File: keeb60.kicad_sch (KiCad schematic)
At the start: 0 parts

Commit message: Add power lines
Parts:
- added U1: nice_nano, symbol nice_nano:nice_nano
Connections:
- new net +5V: U1.21 (VCC)
- new net GND: U1.23 (GND)

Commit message: Add matrix
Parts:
- removed U1: nice_nano, symbol nice_nano:nice_nano
- added D0, D1, D10, D11, D12, D13, D14, D15, D16, D17, D18, D19, D2, D20, D21, D22, D23, D24, D25, D26, D27, D28, D29, D3, D30, D31, D32, D33, D34, D35, D36, D37, D38, D39, D4, D41, D42, D44, D45, D46, D47, D48, D49, D5, D50, D51, D52, D53, D55, D56, D57, D58, D6, D62, D66, D67, D68, D69, D7, D8, D9: D, symbol Device:D
- added K000: Esc, symbol Switch:SW_Push
- added K001: 1, symbol Switch:SW_Push
- added K002: 2, symbol Switch:SW_Push
- added K003: 3, symbol Switch:SW_Push
- added K004: 4, symbol Switch:SW_Push
- added K005: 5, symbol Switch:SW_Push
- added K006: 6, symbol Switch:SW_Push
- added K007: 7, symbol Switch:SW_Push
- added K008: 8, symbol Switch:SW_Push
- added K009: 9, symbol Switch:SW_Push
- added K010: 0, symbol Switch:SW_Push
- added K011: _, symbol Switch:SW_Push
- added K012: =, symbol Switch:SW_Push
- added K013: Backspace, symbol Switch:SW_Push
- added K100: Tab, symbol Switch:SW_Push
- added K101: Q, symbol Switch:SW_Push
- added K102: W, symbol Switch:SW_Push
- added K103: E, symbol Switch:SW_Push
- added K104: R, symbol Switch:SW_Push
- added K105: T, symbol Switch:SW_Push
- added K106: Y, symbol Switch:SW_Push
- added K107: U, symbol Switch:SW_Push
- added K108: I, symbol Switch:SW_Push
- added K109: O, symbol Switch:SW_Push
- added K110: P, symbol Switch:SW_Push
- added K111: [, symbol Switch:SW_Push
- added K112: ], symbol Switch:SW_Push
- added K113: |, symbol Switch:SW_Push
- added K200: Caps Lock, symbol Switch:SW_Push
- added K201: A, symbol Switch:SW_Push
- added K202: S, symbol Switch:SW_Push
- added K203: D, symbol Switch:SW_Push
- added K204: F, symbol Switch:SW_Push
- added K205: G, symbol Switch:SW_Push
- added K206: H, symbol Switch:SW_Push
- added K207: J, symbol Switch:SW_Push
- added K208: K, symbol Switch:SW_Push
- added K209: L, symbol Switch:SW_Push
- added K210: ;, symbol Switch:SW_Push
- added K211, K309: ,, symbol Switch:SW_Push
- added K213: Enter, symbol Switch:SW_Push
- added K300, K313: Shift, symbol Switch:SW_Push
- added K302: Z, symbol Switch:SW_Push
- added K303: X, symbol Switch:SW_Push
- added K304: C, symbol Switch:SW_Push
- added K305: V, symbol Switch:SW_Push
- added K306: B, symbol Switch:SW_Push
- added K307: N, symbol Switch:SW_Push
- added K308: M, symbol Switch:SW_Push
- added K310: ., symbol Switch:SW_Push
- added K311: /, symbol Switch:SW_Push
- added K400, K413: Ctrl, symbol Switch:SW_Push
- added K401, K411: Option, symbol Switch:SW_Push
- added K402, K410: Command, symbol Switch:SW_Push
- added K406: Space, symbol Switch:SW_Push
- added K412: Function, symbol Switch:SW_Push
- added U1: ProMicro, Zodiark:ProMicro_rev2, symbol TheOneProMicro:ProMicro_2-Lily58-cache
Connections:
- new net: D41.2 (A), K213.1
- new net: D15.2 (A), K101.1
- new net: D44.2 (A), K302.1
- new net: D55.2 (A), K313.1
- new net: D45.2 (A), K303.1
- new net: D46.2 (A), K304.1
- new net: D42.2 (A), K300.1
- new net: D30.2 (A), K202.1
- new net: D34.2 (A), K206.1
- new net: D16.2 (A), K102.1
- new net: D4.2 (A), K004.1
- new net: D51.2 (A), K309.1
- new net: D3.2 (A), K003.1
- new net: D67.2 (A), K411.1
- new net: D36.2 (A), K208.1
- new net: D58.2 (A), K402.1
- new net: D62.2 (A), K406.1
- new net: D49.2 (A), K307.1
- new net: D12.2 (A), K012.1
- new net: D28.2 (A), K200.1
- new net: D9.2 (A), K009.1
- new net: D31.2 (A), K203.1
- new net: D57.2 (A), K401.1
- new net: D32.2 (A), K204.1
- new net: D0.2 (A), K000.1
- new net: D66.2 (A), K410.1
- new net: D11.2 (A), K011.1
- new net: D10.2 (A), K010.1
- new net: D8.2 (A), K008.1
- new net: D6.2 (A), K006.1
- new net: D18.2 (A), K104.1
- new net: D47.2 (A), K305.1
- new net: D24.2 (A), K110.1
- new net: D7.2 (A), K007.1
- new net: D52.2 (A), K310.1
- new net: D22.2 (A), K108.1
- new net: D19.2 (A), K105.1
- new net: D68.2 (A), K412.1
- new net: D29.2 (A), K201.1
- new net: D53.2 (A), K311.1
- new net: D26.2 (A), K112.1
- new net: D27.2 (A), K113.1
- new net: D14.2 (A), K100.1
- new net: D17.2 (A), K103.1
- new net: D39.2 (A), K211.1
- new net: D37.2 (A), K209.1
- new net: D2.2 (A), K002.1
- new net: D21.2 (A), K107.1
- new net: D5.2 (A), K005.1
- new net: D56.2 (A), K400.1
- new net: D48.2 (A), K306.1
- new net: D25.2 (A), K111.1
- new net: D20.2 (A), K106.1
- new net: D33.2 (A), K205.1
- new net: D35.2 (A), K207.1
- new net: D23.2 (A), K109.1
- new net: D38.2 (A), K210.1
- new net: D13.2 (A), K013.1
- new net: D50.2 (A), K308.1
- new net: D1.2 (A), K001.1
- new net: D69.2 (A), K413.1
- new net Col0: K000.2, K100.2, K200.2, K300.2, K400.2, U1.1 (GP0(TX))
- new net Col1: K001.2, K101.2, K201.2, K401.2, U1.2 (GP1(RX))
- new net Col10: K010.2, K110.2, K210.2, K310.2, K410.2, U1.17 (GP26(A0))
- new net Col11: K011.2, K111.2, K211.2, K311.2, K411.2, U1.18 (GP27(A1))
- new net Col12: K012.2, K112.2, K412.2, U1.19 (GP28(A2))
- new net Col13: K013.2, K113.2, K213.2, K313.2, K413.2, U1.20 (GP29(A3))
- new net Col2: K002.2, K102.2, K202.2, K302.2, K402.2, U1.5 (SDA(GP2))
- new net Col3: K003.2, K103.2, K203.2, K303.2, U1.6 (SCL(GP3))
- new net Col4: K004.2, K104.2, K204.2, K304.2, U1.7 (GP4)
- new net Col5: K005.2, K105.2, K205.2, K305.2, U1.8 (GP5)
- new net Col6: K006.2, K106.2, K206.2, K306.2, K406.2, U1.9 (GP6)
- new net Col7: K007.2, K107.2, K207.2, K307.2, U1.14 (GP23)
- new net Col8: K008.2, K108.2, K208.2, K308.2, U1.15 (GP20)
- new net Col9: K009.2, K109.2, K209.2, K309.2, U1.16 (GP22)
- new net Row0: D0.1 (K), D1.1 (K), D10.1 (K), D11.1 (K), D12.1 (K), D13.1 (K), D2.1 (K), D3.1 (K), D4.1 (K), D5.1 (K), D6.1 (K), D7.1 (K), D8.1 (K), D9.1 (K), U1.10 (GP7)
- new net Row1: D14.1 (K), D15.1 (K), D16.1 (K), D17.1 (K), D18.1 (K), D19.1 (K), D20.1 (K), D21.1 (K), D22.1 (K), D23.1 (K), D24.1 (K), D25.1 (K), D26.1 (K), D27.1 (K), U1.11 (GP8)
- new net Row2: D28.1 (K), D29.1 (K), D30.1 (K), D31.1 (K), D32.1 (K), D33.1 (K), D34.1 (K), D35.1 (K), D36.1 (K), D37.1 (K), D38.1 (K), D39.1 (K), D41.1 (K), U1.12 (GP9)
- new net Row3: D42.1 (K), D44.1 (K), D45.1 (K), D46.1 (K), D47.1 (K), D48.1 (K), D49.1 (K), D50.1 (K), D51.1 (K), D52.1 (K), D53.1 (K), D55.1 (K), U1.13 (GP21)
- new net Row4: D56.1 (K), D57.1 (K), D58.1 (K), D62.1 (K), D66.1 (K), D67.1 (K), D68.1 (K), D69.1 (K)

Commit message: Start assigning footprints
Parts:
- K000, K001: footprint (none) -> MX_Hotswap:MX-Hotswap-1U
- U1: footprint Zodiark:ProMicro_rev2 -> TheOneProMicro-main:TheOneProMicro
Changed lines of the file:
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@@
 			)
 		)
-		(property "Footprint" ""
+		(property "Footprint" "MX_Hotswap:MX-Hotswap-1U"
 			(at 57.15 78.74 0)
 			(effects
@@
 			)
 		)
-		(property "Footprint" "Zodiark:ProMicro_rev2"
+		(property "Footprint" "TheOneProMicro-main:TheOneProMicro"
 			(at 38.1 41.91 0)
 			(effects
@@
 			)
 		)
-		(property "Footprint" ""
+		(property "Footprint" "MX_Hotswap:MX-Hotswap-1U"
 			(at 72.39 78.74 0)
 			(effects

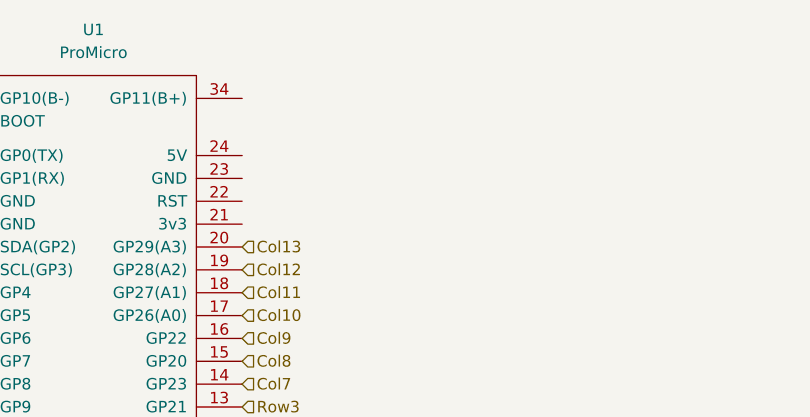
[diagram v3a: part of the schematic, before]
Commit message: Add footprints
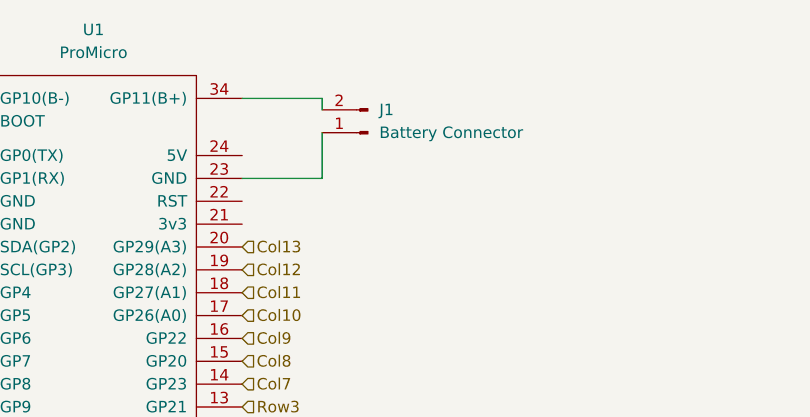
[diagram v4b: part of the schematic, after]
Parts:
- added J1: Battery Connector, Connector_JST:JST_XH_B2B-XH-A_1x02_P2.50mm_Vertical, symbol Connector:Conn_01x02_Pin
- D0, D1, D10, D11, D12, D13, D14, D15, D16, D17, D18, D19, D2, D20, D21, D22, D23, D24, D25, D26, D27, D28, D29, D3, D30, D31, D32, D33, D34, D35, D36, D37, D38, D39, D4, D41, D42, D44, D45, D46, D47, D48, D49, D5, D50, D51, D52, D53, D55, D56, D57, D58, D6, D62, D66, D67, D68, D69, D7, D8, D9: footprint (none) -> Diode_THT:D_DO-35_SOD27_P7.62mm_Horizontal
- K002, K003, K004, K005, K006, K007, K008, K009, K010, K011, K012, K101, K102, K103, K104, K105, K106, K107, K108, K109, K110, K111, K112, K201, K202, K203, K204, K205, K206, K207, K208, K209, K210, K211, K302, K303, K304, K305, K306, K307, K308, K309, K310, K311: footprint (none) -> MX_Hotswap:MX-Hotswap-1U
- K013: footprint (none) -> MX_Hotswap:MX-Hotswap-2U
- K100, K113: footprint (none) -> MX_Hotswap:MX-Hotswap-1.5U
- K200: footprint (none) -> MX_Hotswap:MX-Hotswap-1.75U
- K213, K300: footprint (none) -> MX_Hotswap:MX-Hotswap-2.25U
- K313: footprint (none) -> MX_Hotswap:MX-Hotswap-2.75U
- K400, K401, K402, K410, K411, K412, K413: footprint (none) -> MX_Hotswap:MX-Hotswap-1.25U
- K406: footprint (none) -> MX_Hotswap:MX-Hotswap-6.25U-ReversedStabilizers
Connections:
- net at U1.23 (GND): now also J1.1 (Pin_1)
- net at U1.34 (GP11(B+)): now also J1.2 (Pin_2)

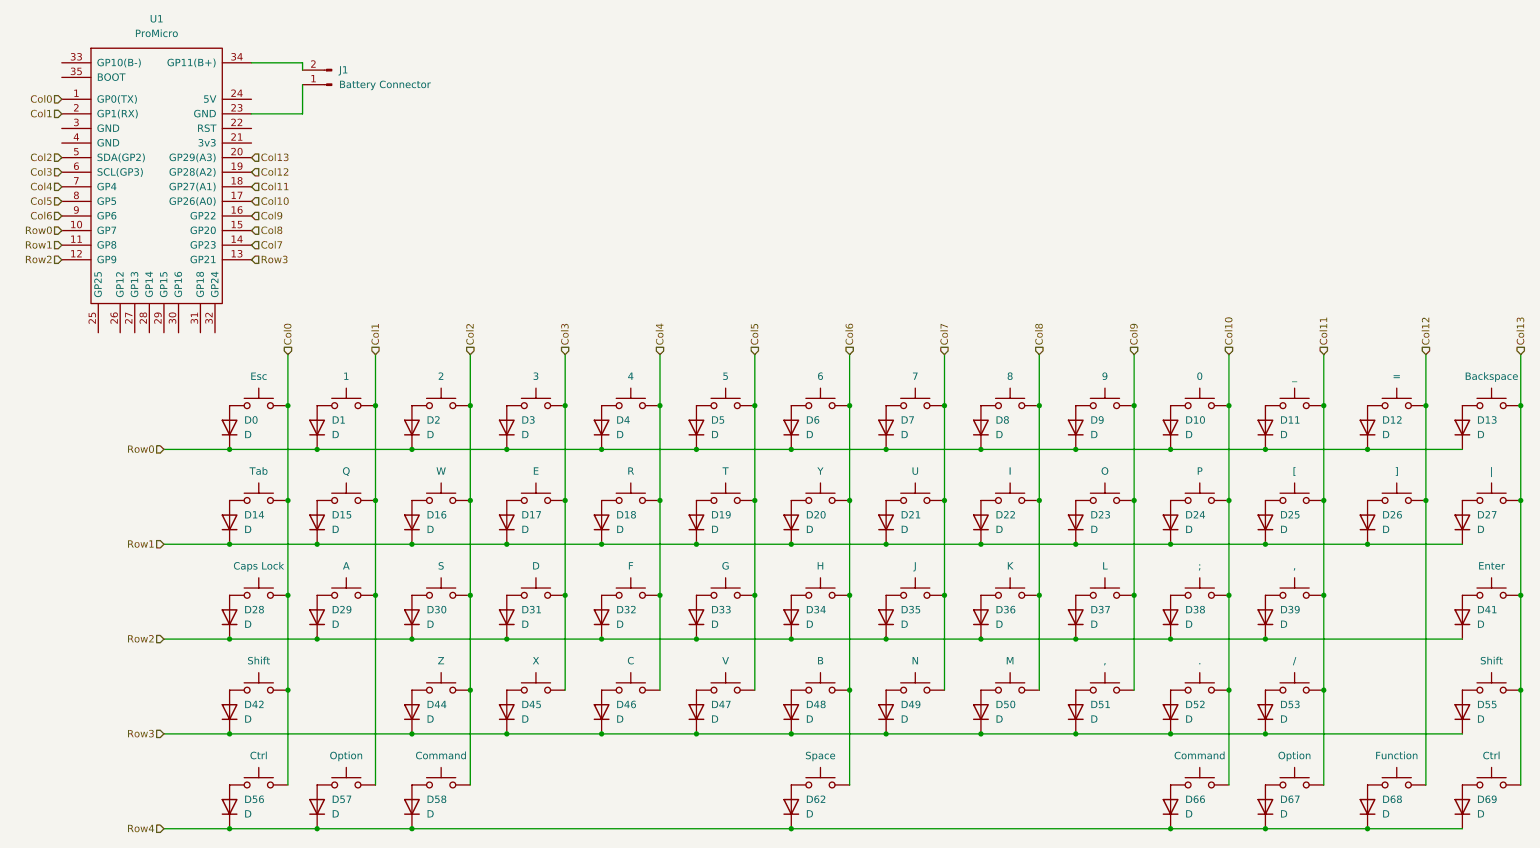
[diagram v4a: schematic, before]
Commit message: Switch to SMA diodes, start laying out board
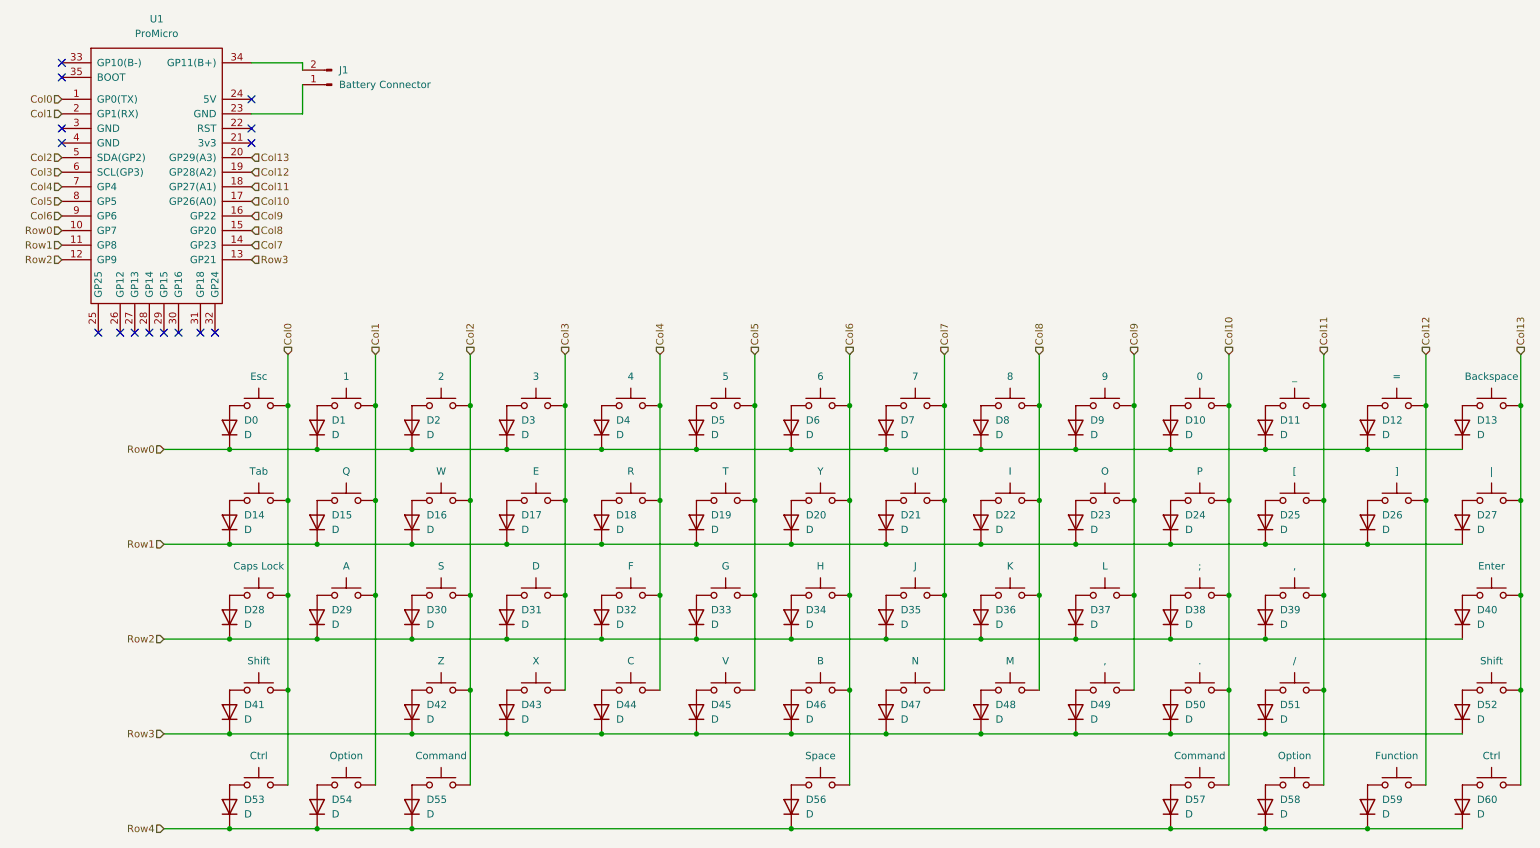
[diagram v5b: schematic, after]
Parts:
- D0, D1, D10, D11, D12, D13, D14, D15, D16, D17, D18, D19, D2, D20, D21, D22, D23, D24, D25, D26, D27, D28, D29, D3, D30, D31, D32, D33, D34, D35, D36, D37, D38, D39, D4, D5, D6, D7, D8, D9: footprint Diode_THT:D_DO-35_SOD27_P7.62mm_Horizontal -> Diode_SMD:D_SOD-123
- D40: renamed from D41; footprint Diode_THT:D_DO-35_SOD27_P7.62mm_Horizontal -> Diode_SMD:D_SOD-123
- D41: renamed from D42; footprint Diode_THT:D_DO-35_SOD27_P7.62mm_Horizontal -> Diode_SMD:D_SOD-123
- D42: renamed from D44; footprint Diode_THT:D_DO-35_SOD27_P7.62mm_Horizontal -> Diode_SMD:D_SOD-123
- D43: renamed from D45; footprint Diode_THT:D_DO-35_SOD27_P7.62mm_Horizontal -> Diode_SMD:D_SOD-123
- D44: renamed from D46; footprint Diode_THT:D_DO-35_SOD27_P7.62mm_Horizontal -> Diode_SMD:D_SOD-123
- D45: renamed from D47; footprint Diode_THT:D_DO-35_SOD27_P7.62mm_Horizontal -> Diode_SMD:D_SOD-123
- D46: renamed from D48; footprint Diode_THT:D_DO-35_SOD27_P7.62mm_Horizontal -> Diode_SMD:D_SOD-123
- D47: renamed from D49; footprint Diode_THT:D_DO-35_SOD27_P7.62mm_Horizontal -> Diode_SMD:D_SOD-123
- D48: renamed from D50; footprint Diode_THT:D_DO-35_SOD27_P7.62mm_Horizontal -> Diode_SMD:D_SOD-123
- D49: renamed from D51; footprint Diode_THT:D_DO-35_SOD27_P7.62mm_Horizontal -> Diode_SMD:D_SOD-123
- D50: renamed from D52; footprint Diode_THT:D_DO-35_SOD27_P7.62mm_Horizontal -> Diode_SMD:D_SOD-123
- D51: renamed from D53; footprint Diode_THT:D_DO-35_SOD27_P7.62mm_Horizontal -> Diode_SMD:D_SOD-123
- D52: renamed from D55; footprint Diode_THT:D_DO-35_SOD27_P7.62mm_Horizontal -> Diode_SMD:D_SOD-123
- D53: renamed from D56; footprint Diode_THT:D_DO-35_SOD27_P7.62mm_Horizontal -> Diode_SMD:D_SOD-123
- D54: renamed from D57; footprint Diode_THT:D_DO-35_SOD27_P7.62mm_Horizontal -> Diode_SMD:D_SOD-123
- D55: renamed from D58; footprint Diode_THT:D_DO-35_SOD27_P7.62mm_Horizontal -> Diode_SMD:D_SOD-123
- D56: renamed from D62; footprint Diode_THT:D_DO-35_SOD27_P7.62mm_Horizontal -> Diode_SMD:D_SOD-123
- D57: renamed from D66; footprint Diode_THT:D_DO-35_SOD27_P7.62mm_Horizontal -> Diode_SMD:D_SOD-123
- D58: renamed from D67; footprint Diode_THT:D_DO-35_SOD27_P7.62mm_Horizontal -> Diode_SMD:D_SOD-123
- D59: renamed from D68; footprint Diode_THT:D_DO-35_SOD27_P7.62mm_Horizontal -> Diode_SMD:D_SOD-123
- D60: renamed from D69; footprint Diode_THT:D_DO-35_SOD27_P7.62mm_Horizontal -> Diode_SMD:D_SOD-123
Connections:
- no-connect marks 0 -> 15

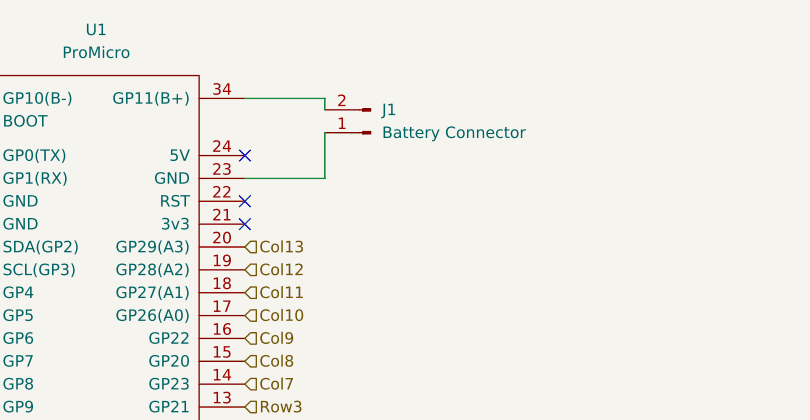
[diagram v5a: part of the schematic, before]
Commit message: Remove JST from board
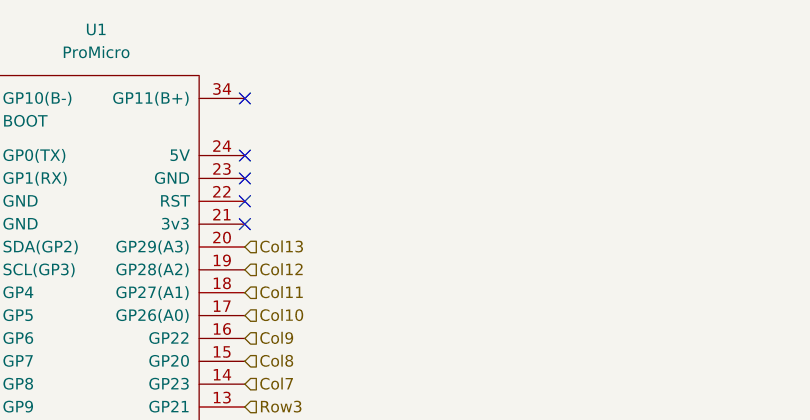
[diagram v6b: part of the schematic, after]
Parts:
- removed J1: Battery Connector, Connector_JST:JST_XH_B2B-XH-A_1x02_P2.50mm_Vertical, symbol Connector:Conn_01x02_Pin
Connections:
- no-connect marks 15 -> 17
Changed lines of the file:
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@@
 	)
 	(no_connect
+		(at 55.88 33.02)
+	)
+	(no_connect
 		(at 40.64 71.12)
 	)
@@
 	)
 	(no_connect
+		(at 55.88 24.13)
+	)
+	(no_connect
 		(at 49.53 71.12)
 	)
@@
 	(wire
 		(pts
-			(xy 55.88 33.02) (xy 64.77 33.02)
-		)
-		(stroke
-			(width 0)
-			(type default)
-		)
-	)
-	(wire
-		(pts
 			(xy 242.57 133.35) (xy 242.57 149.86)
 		)
@@
 	(wire
 		(pts
-			(xy 55.88 24.13) (xy 64.77 24.13)
-		)
-		(stroke
-			(width 0)
-			(type default)
-		)
-	)
-	(wire
-		(pts
 			(xy 232.41 157.48) (xy 250.19 157.48)
 		)
@@
 	(wire
 		(pts
-			(xy 64.77 24.13) (xy 64.77 25.4)
-		)
-		(stroke
-			(width 0)
-			(type default)
-		)
-	)
-	(wire
-		(pts
 			(xy 176.53 74.93) (xy 176.53 83.82)
 		)
@@
 	(wire
 		(pts
-			(xy 64.77 27.94) (xy 64.77 33.02)
-		)
-		(stroke
-			(width 0)
-			(type default)
-		)
-	)
-	(wire
-		(pts
 			(xy 62.23 100.33) (xy 62.23 116.84)
 		)
@@
 					(unit 1)
 				)
-			)
-		)
-	)
-	(symbol
-		(lib_id "Connector:Conn_01x02_Pin")
-		(at 69.85 27.94 180)
-		(unit 1)
-		(exclude_from_sim no)
-		(in_bom yes)
-		(on_board yes)
-		(dnp no)
-		(fields_autoplaced yes)
-		(property "Reference" "J1"
-			(at 71.12 25.3999 0)
-			(effects
-				(font
-					(size 1.27 1.27)
-				)
-				(justify right)
-			)
-		)
-		(property "Value" "Battery Connector"
-			(at 71.12 27.9399 0)
-			(effects
-				(font
-					(size 1.27 1.27)
-				)
-				(justify right)
-			)
-		)
-		(property "Footprint" "Connector_JST:JST_XH_B2B-XH-A_1x02_P2.50mm_Vertical"
-			(at 69.85 27.94 0)
-			(effects
-				(font
-					(size 1.27 1.27)
-				)
-				(hide yes)
-			)
-		)
-		(property "Datasheet" "~"
-			(at 69.85 27.94 0)
-			(effects
-				(font
-					(size 1.27 1.27)
-				)
-				(hide yes)
-			)
-		)
-		(property "Description" "Generic connector, single row, 01x02, script generated"
-			(at 69.85 27.94 0)
-			(effects
-				(font
-					(size 1.27 1.27)
-				)
-				(hide yes)
-			)
-		)
-		(pin "2"
-		)
-		(pin "1"
-		)
-		(instances
-			(project ""
-				(path "/352791af-23f7-4e44-a171-c4b3d1d94775"
-					(reference "J1")
-					(unit 1)
-				)
